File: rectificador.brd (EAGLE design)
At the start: 64 x 71.1 mm, 26 parts, among them T1 TYN612, X2 X2

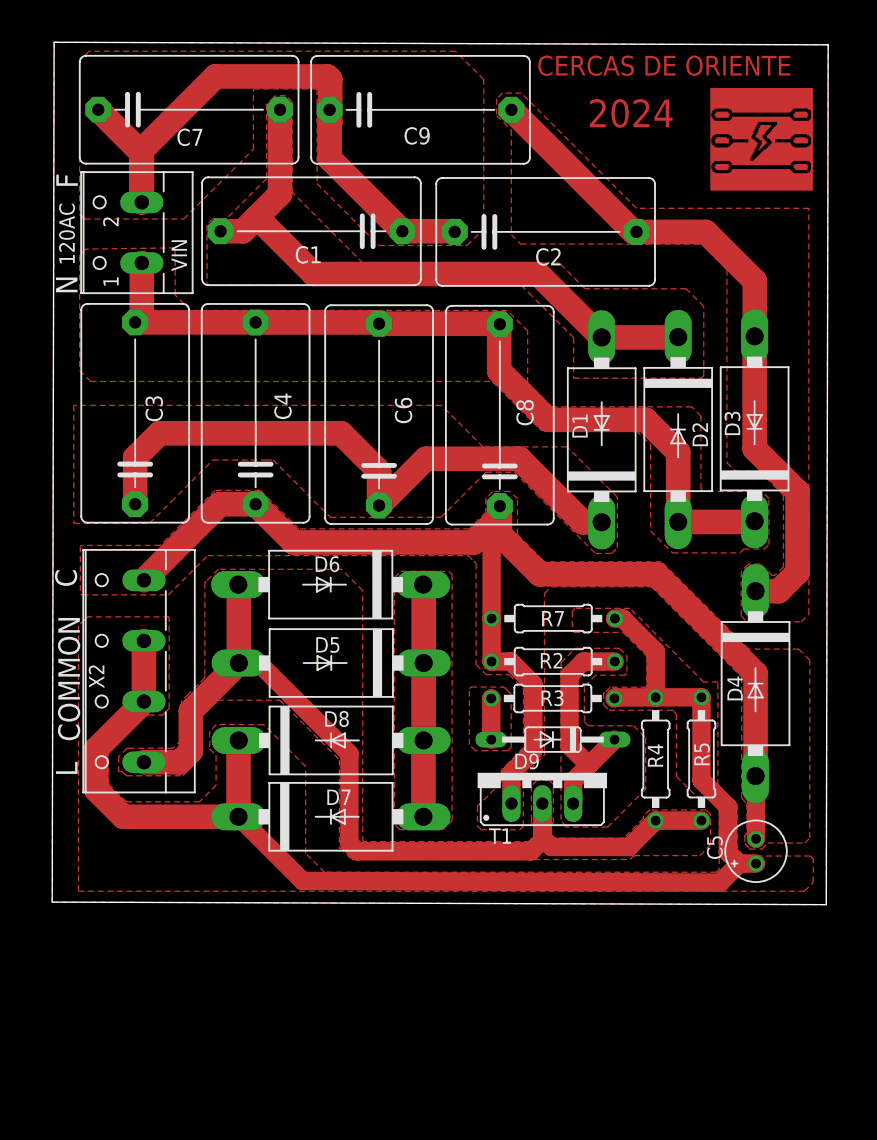
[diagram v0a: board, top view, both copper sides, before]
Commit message: feat: add 3D packages.
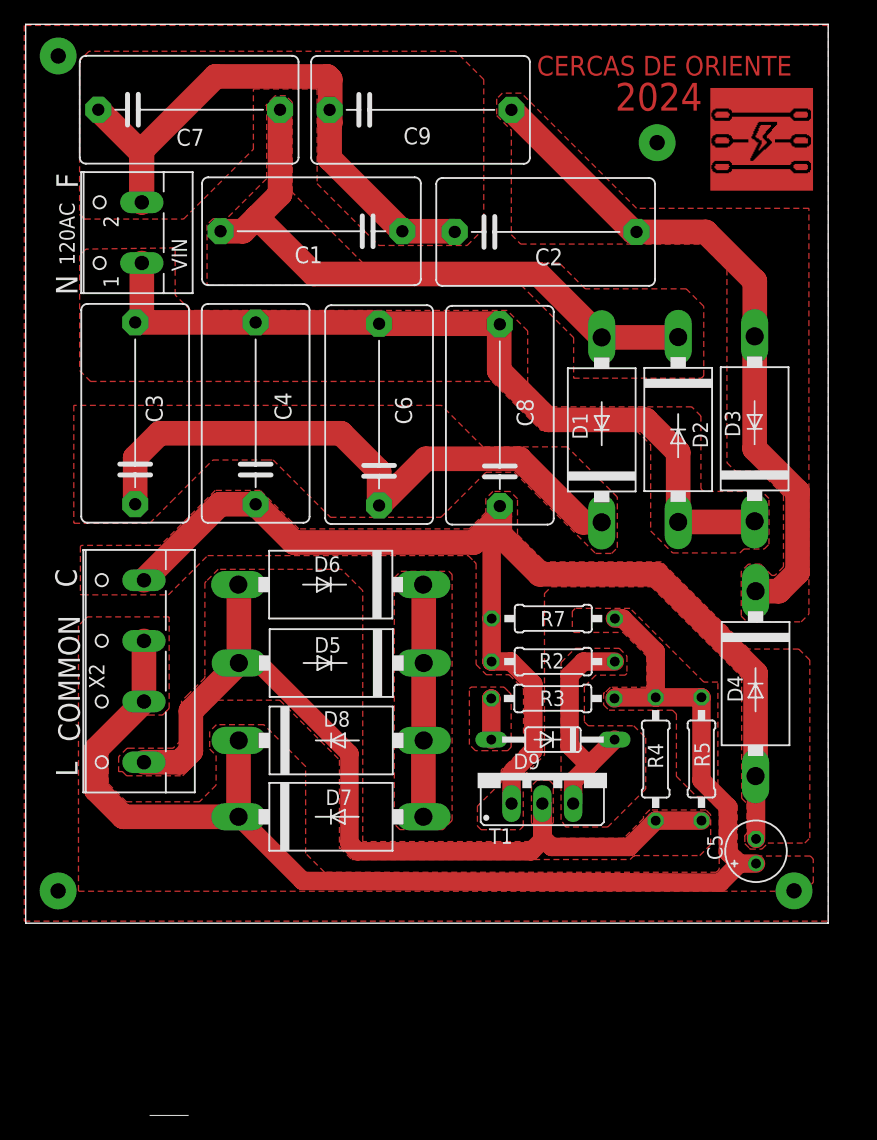
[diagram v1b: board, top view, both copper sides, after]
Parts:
- C1, C2, C4, C6: value (none) -> 225J400
- C3, C7, C8, C9: value (none) -> 335J400V
- C5: value (none) -> 47u
- R3: value (none) -> 470
- R4: value (none) -> 2M
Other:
- board size 64 x 71.1 mm -> 66.2 x 74.1 mm
